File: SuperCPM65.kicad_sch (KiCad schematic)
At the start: 35 parts, among them CON1 db_vgparts_SNES-EDGE, J1 GSD090012SEU, J2 Mini-DIN-6, J3 Conn_01x06, U1 TXB0104D, U2 W65C22NxP, U3 AP2205-33W5-7, U4 74HC14, U5 74HC595, U6 74HC595, U8 PIC12F629-IP, U9 SST39SF010

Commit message: Fixed some 3D model issues and socketed the PIC
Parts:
- U8: footprint Package_DIP:DIP-8_W7.62mm -> Package_DIP:DIP-8_W7.62mm_Socket
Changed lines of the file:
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@@
 			)
 		)
-		(property "Footprint" "Package_DIP:DIP-8_W7.62mm"
+		(property "Footprint" "Package_DIP:DIP-8_W7.62mm_Socket"
 			(at 156.21 21.59 0)
 			(effects

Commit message: Added LEDs for CE signals, header for leftover VIA I/Os, changed addressing to allow larger Flash memory and added a jumper for Flash memory write enable
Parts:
- added D7, D8: LED, LED_SMD:LED_0805_2012Metric, symbol Device:LED
- added J4: Conn_01x02, Connector_PinHeader_2.54mm:PinHeader_1x02_P2.54mm_Vertical, symbol Connector_Generic:Conn_01x02
- added J5: Conn_01x06, Connector_PinHeader_2.54mm:PinHeader_1x06_P2.54mm_Vertical, symbol Connector_Generic:Conn_01x06
- added R4, R5: 1k, Resistor_SMD:R_0805_2012Metric_Pad1.20x1.40mm_HandSolder, symbol Device:R
- added R8: 10k, Resistor_SMD:R_0805_2012Metric_Pad1.20x1.40mm_HandSolder, symbol Device:R
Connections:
- net +5V: now also J5.1 (Pin_1), R8.1; no longer U9.31 (PGM)
- net BA1: now also U9.30 (NC); no longer D4.2 (A), U4.9
- net GND: now also J5.6 (Pin_6), R4.2, R5.2; no longer U4.11, U4.13
- net ~{CE_ROM}: now also U4.11
- net ~{CE_VIA}: now also U4.13
- net ~{WR}: now also J4.2 (Pin_2)
- net BA2: now reaches CON1.43 (BA2)
- net BA2: now also U9.1 (NC)
- net BA3: now reaches CON1.44 (BA3)
- net BA3: now also D4.2 (A), U4.9
- net PA0: now reaches U2.2 (PA0)
- net PA0: now also J5.2 (Pin_2)
- net PA5: now reaches U2.7 (PA5)
- net PA5: now also J5.3 (Pin_3)
- net PA6: now reaches U2.8 (PA6)
- net PA6: now also J5.4 (Pin_4)
- net PA7: now reaches U2.9 (PA7)
- net PA7: now also J5.5 (Pin_5)
- net at U4.12: now also D7.2 (A)
- net at U4.10: now also D8.2 (A)
- new net: J4.1 (Pin_1), R8.2, U9.31 (PGM)
- new net: D8.1 (K), R5.1
- new net: D7.1 (K), R4.1
- no-connect marks 27 -> 23
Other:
- note removed: "Image select jumpers"
- moved on the sheet: J1, U4E, U4F

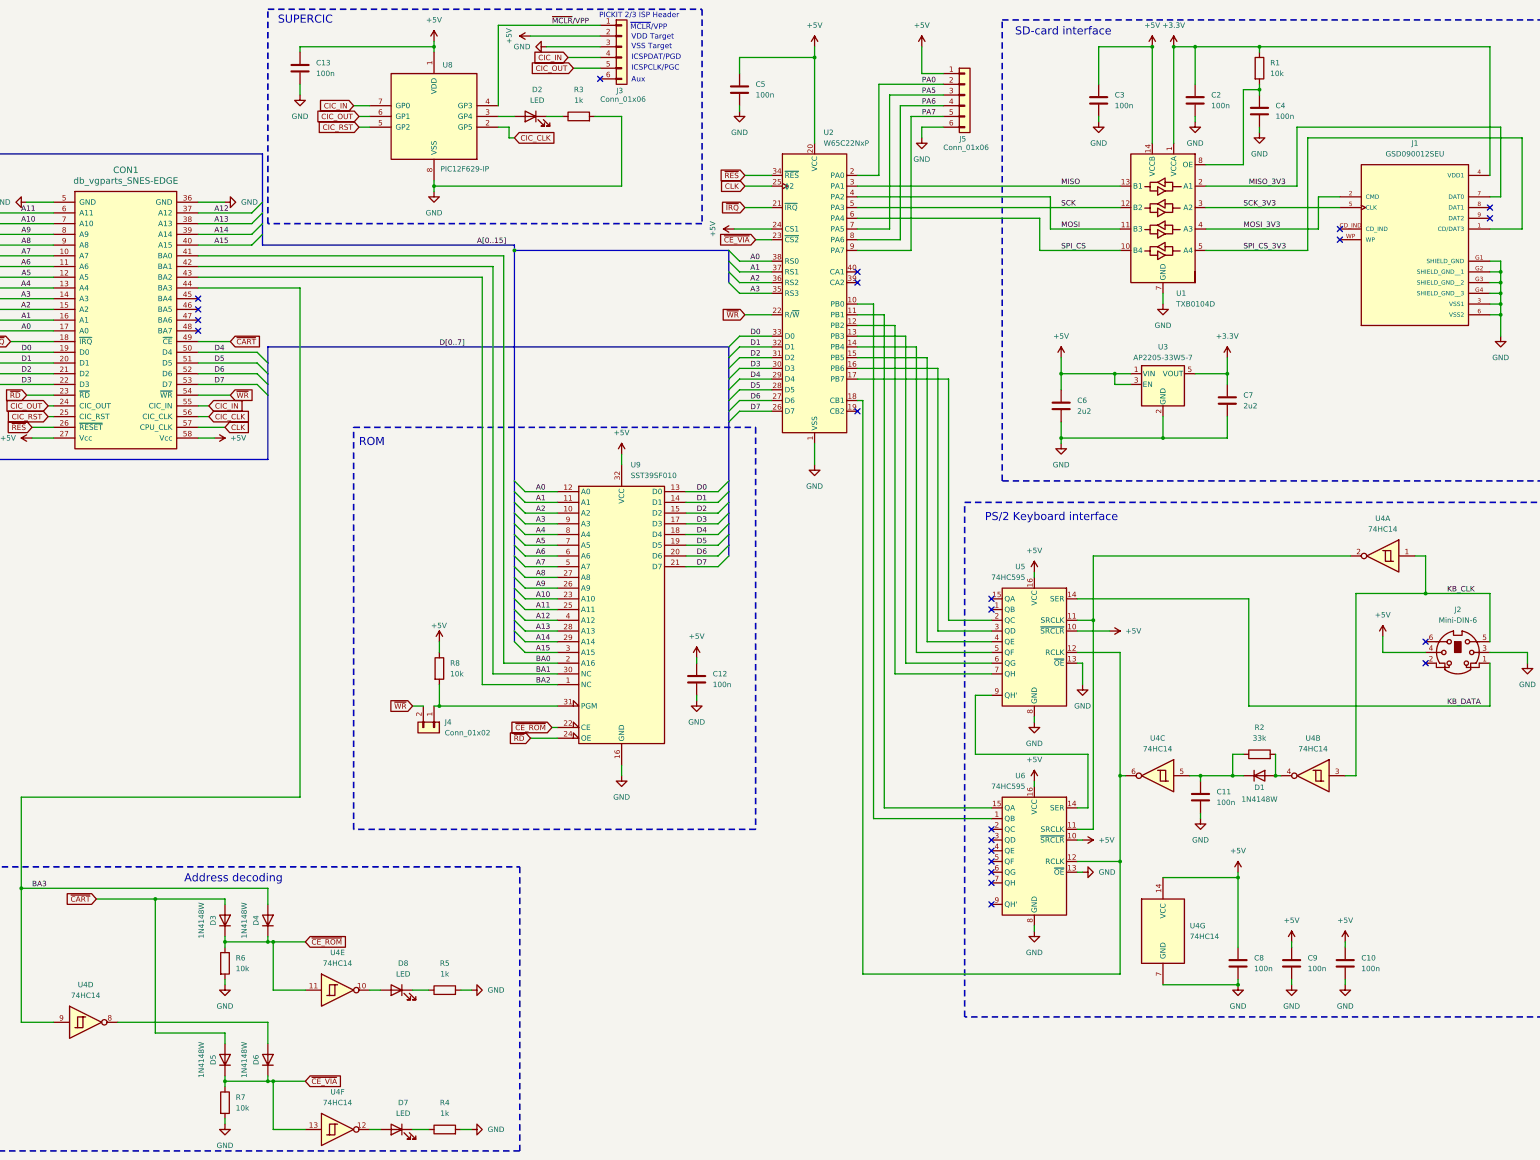
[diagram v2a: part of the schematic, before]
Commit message: Reset component annotation as some components were removed
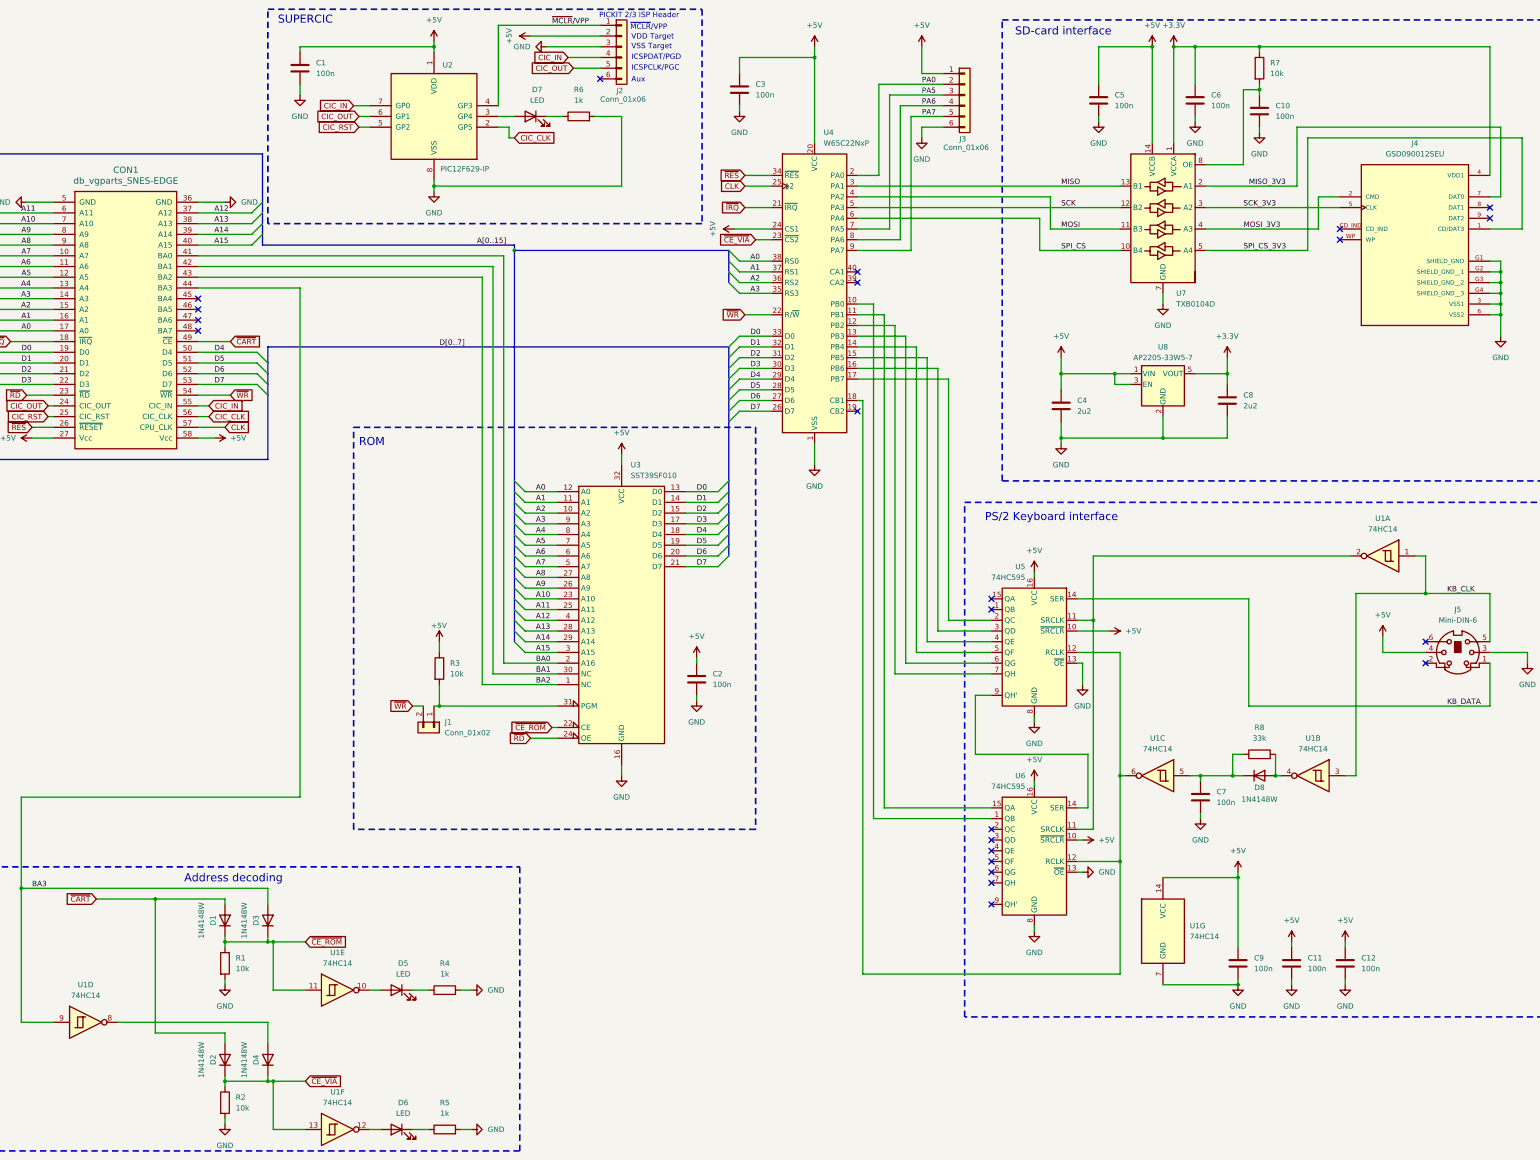
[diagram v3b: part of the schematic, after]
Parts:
- renumbered C13 to C1, C4 to C10, C9 to C11, C10 to C12, C12 to C2, C5 to C3, C6 to C4, C3 to C5, C2 to C6, C11 to C7, C7 to C8, C8 to C9, D3 to D1, D5 to D2, D4 to D3, D6 to D4, D8 to D5, D7 to D6, D2 to D7, D1 to D8, J4 to J1, J3 to J2, J5 to J3, J1 to J4, J2 to J5, R6 to R1, R7 to R2, R8 to R3, R5 to R4, R4 to R5, R3 to R6, R1 to R7, R2 to R8, U4 to U1, U8 to U2, U9 to U3, U2 to U4, U1 to U7, U3 to U8

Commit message: Updated BOM
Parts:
- J1: Supplier (none) -> Mouser; Supplier P/N (none) -> 538-22-28-4027
- J2, J3: Supplier P/N 855-M20-9750642 -> 538-22-28-4061
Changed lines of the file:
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@@
 			)
 		)
+		(property "Supplier" "Mouser"
+			(at 140.97 182.88 0)
+			(effects
+				(font
+					(size 1.27 1.27)
+				)
+				(hide yes)
+			)
+		)
+		(property "Supplier P/N" "538-22-28-4027"
+			(at 140.97 182.88 0)
+			(effects
+				(font
+					(size 1.27 1.27)
+				)
+				(hide yes)
+			)
+		)
 		(pin "2"
 		)
@@
 			)
 		)
-		(property "Supplier P/N" "855-M20-9750642 "
+		(property "Supplier P/N" "538-22-28-4061"
 			(at 266.7 33.02 0)
 			(effects
@@
 			)
 		)
-		(property "Supplier P/N" "855-M20-9750642 "
+		(property "Supplier P/N" "538-22-28-4061"
 			(at 185.42 21.59 0)
 			(effects

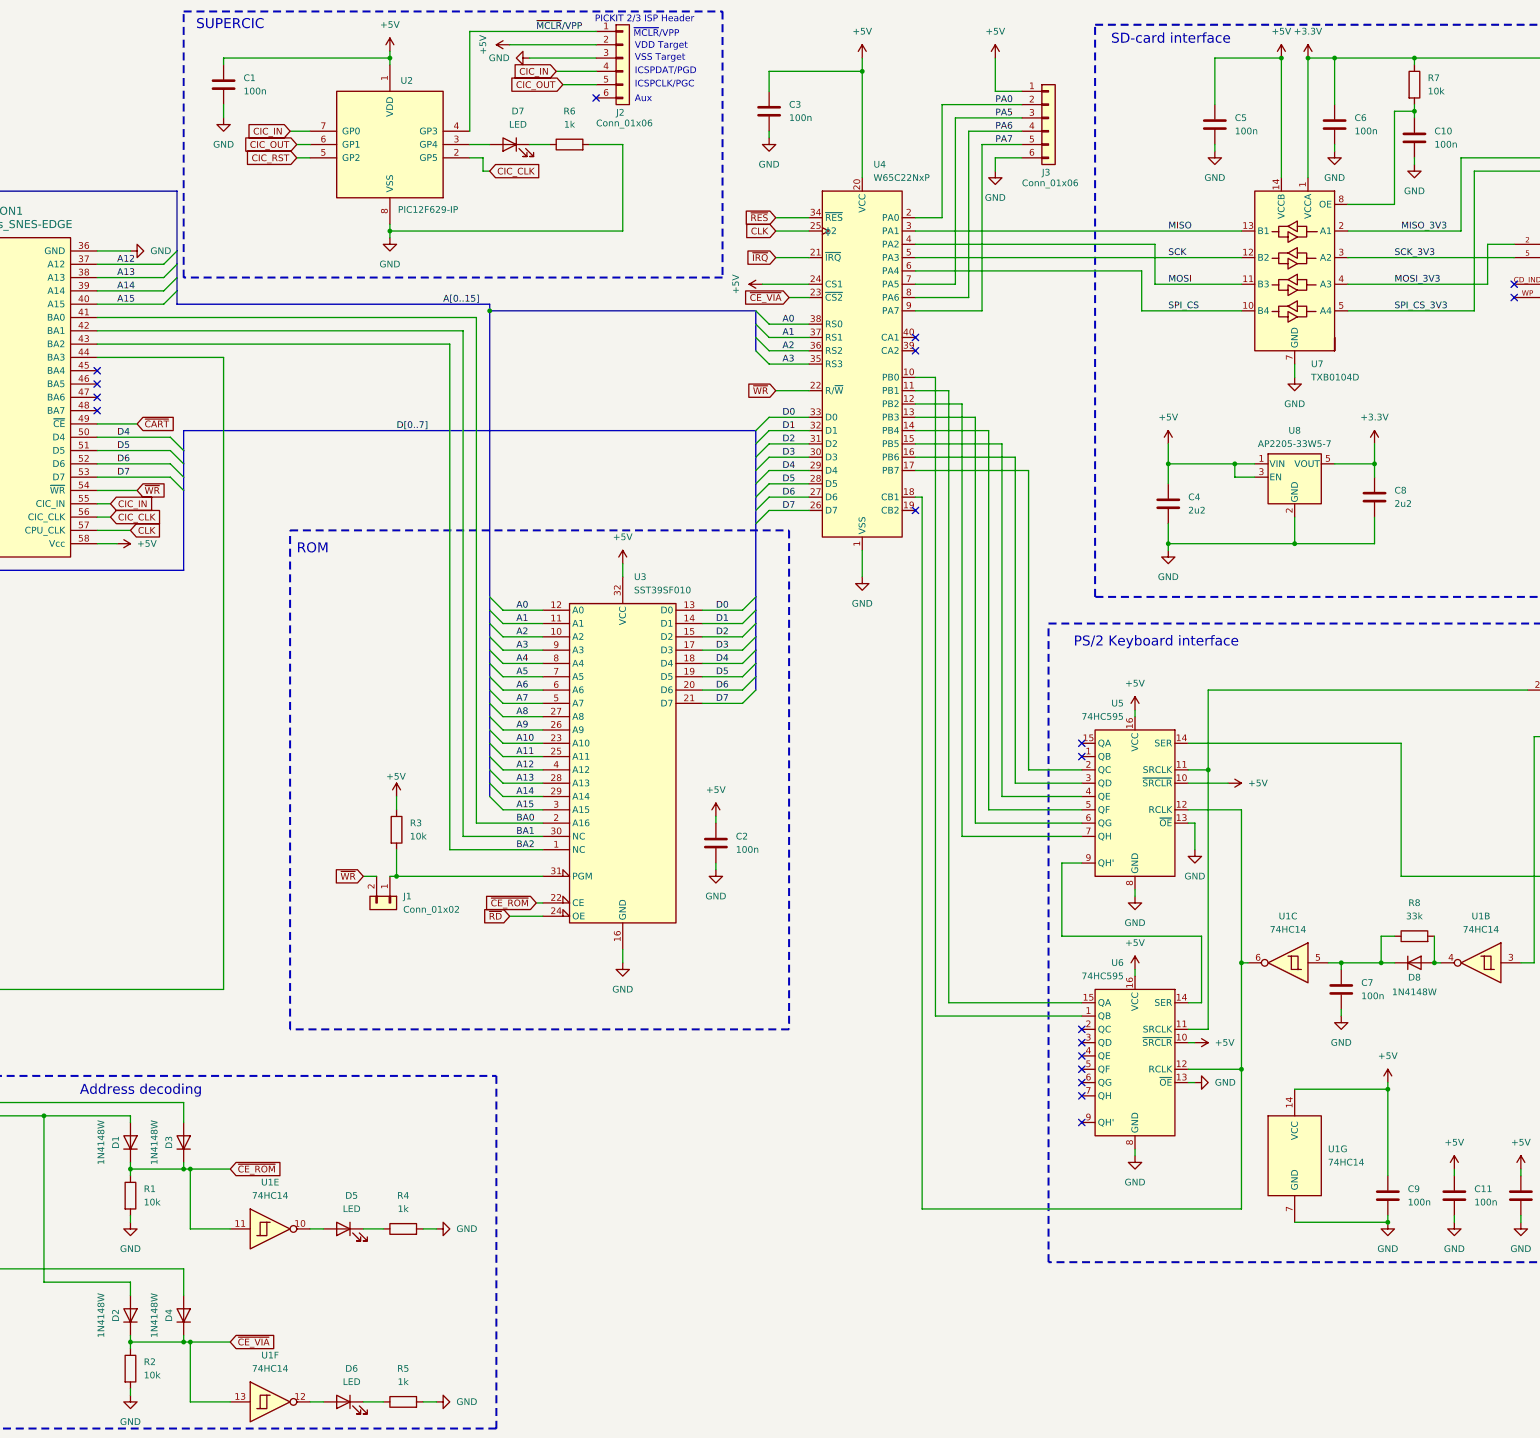
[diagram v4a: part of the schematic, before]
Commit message: Added more signals to VIA spare header. Added diode to IRQ line. Changed all diodes to schottky
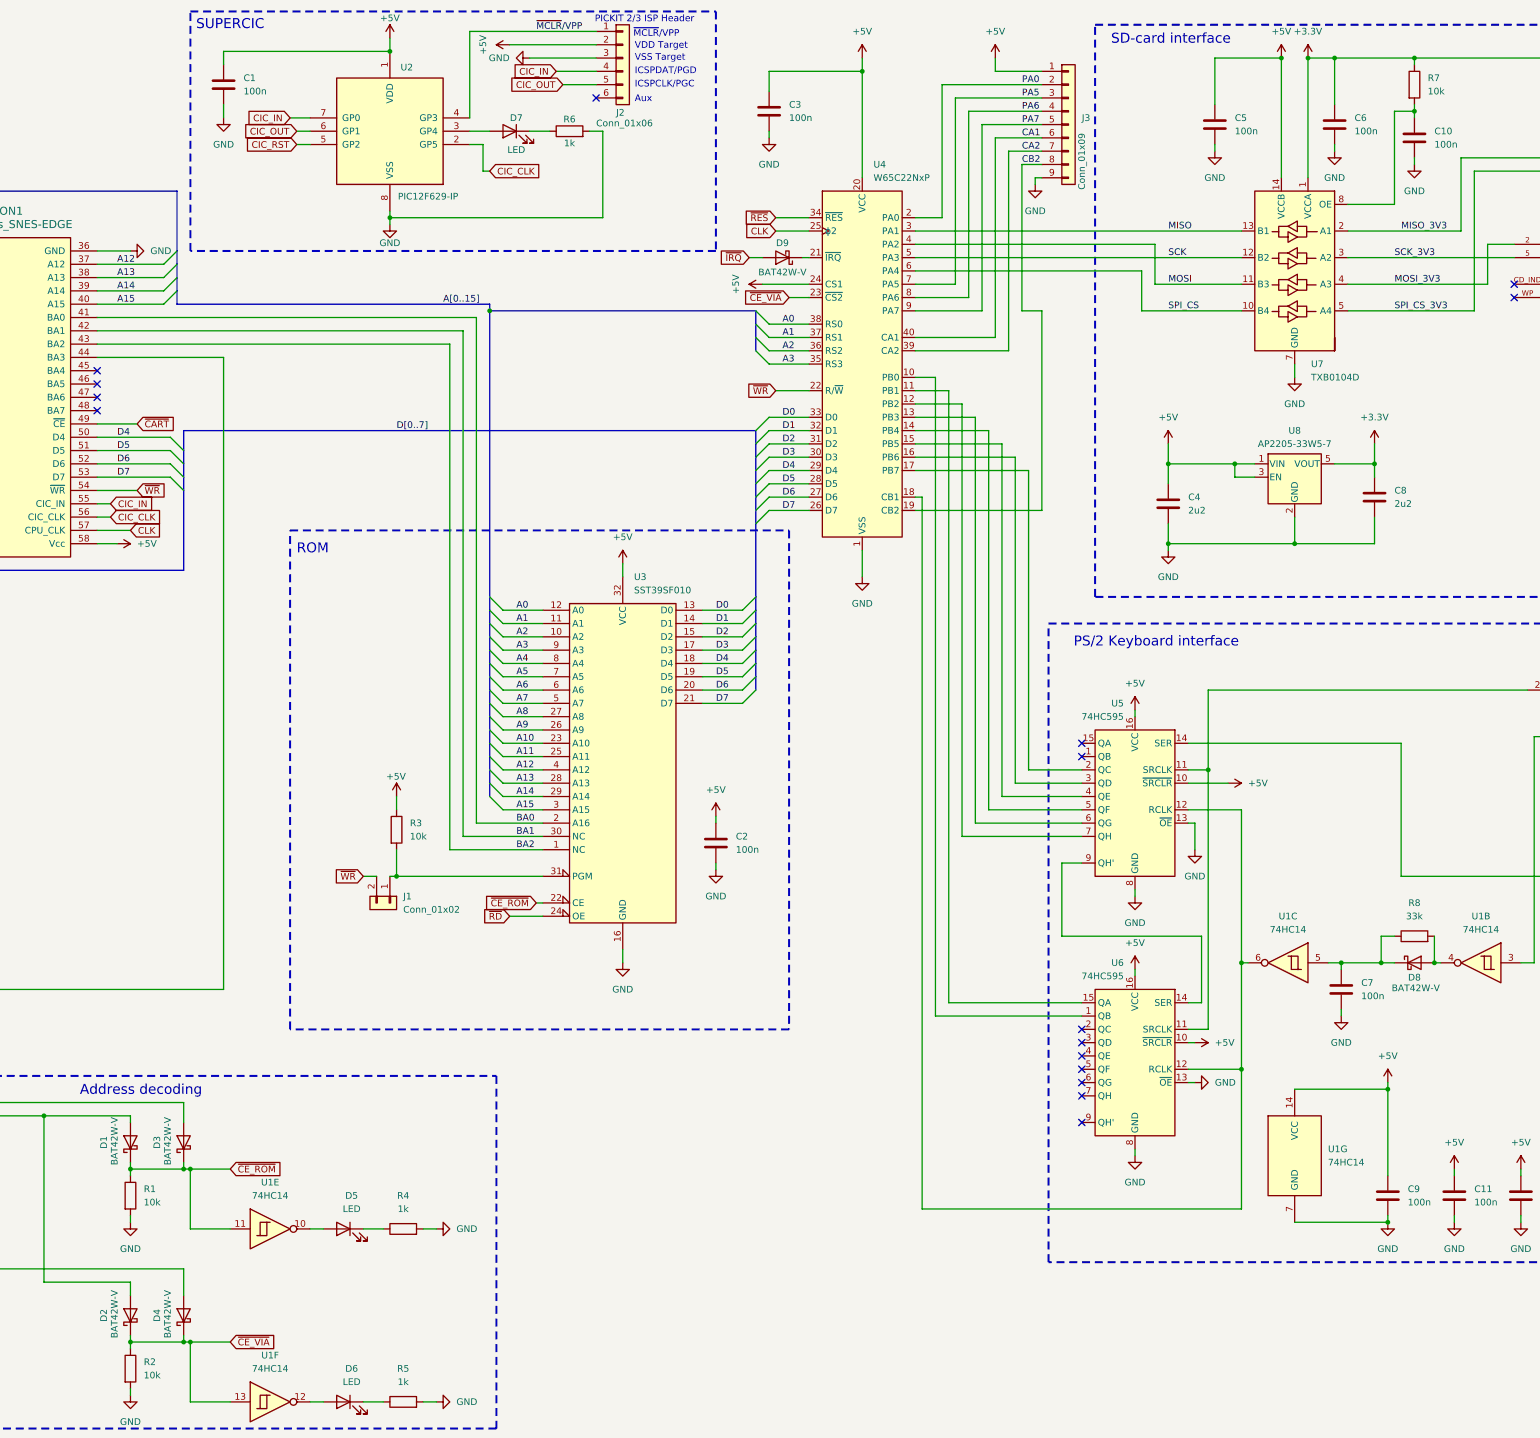
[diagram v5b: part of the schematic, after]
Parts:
- removed D1, D2, D3, D4, D8: 1N4148W, Diode_SMD:D_SOD-123, symbol Diode:1N4148W
- removed J3: Conn_01x06, Connector_PinHeader_2.54mm:PinHeader_1x06_P2.54mm_Vertical, symbol Connector_Generic:Conn_01x06
- added D1, D2, D3, D4, D8, D9: BAT42W-V, Diode_SMD:D_SOD-123, symbol Diode:BAT42W-V
- added J3: Conn_01x09, Connector_PinHeader_2.54mm:PinHeader_1x09_P2.54mm_Vertical, symbol Connector_Generic:Conn_01x09
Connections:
- net +5V: now also J3.1 (Pin_1)
- net BA3: now also D3.2 (A)
- net GND: now also J3.9 (Pin_9)
- net PA0: now also J3.2 (Pin_2)
- net PA5: now also J3.3 (Pin_3)
- net PA6: now also J3.4 (Pin_4)
- net PA7: now also J3.5 (Pin_5)
- net ~{CART}: now also D1.2 (A), D2.2 (A)
- net ~{CE_ROM}: now also D1.1 (K), D3.1 (K)
- net ~{CE_VIA}: now also D2.1 (K), D4.1 (K)
- net ~{IRQ}: now also D9.2 (A); no longer U4.21 (~{IRQ})
- net at U1.8: now also D4.2 (A)
- net at C7.1, R8.1, U1.5: now also D8.1 (K)
- net at R8.2, U1.4: now also D8.2 (A)
- net CB2: now reaches U4.19 (CB2)
- net CB2: now also J3.8 (Pin_8)
- net CA2: now reaches U4.39 (CA2)
- net CA2: now also J3.7 (Pin_7)
- net CA1: now reaches U4.40 (CA1)
- net CA1: now also J3.6 (Pin_6)
- new net: D9.1 (K), U4.21 (~{IRQ})
- no-connect marks 23 -> 20
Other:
- moved on the sheet: D7, R6, U2
